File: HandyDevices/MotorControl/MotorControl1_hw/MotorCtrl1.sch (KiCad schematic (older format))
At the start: 20 parts, among them U1 L6470

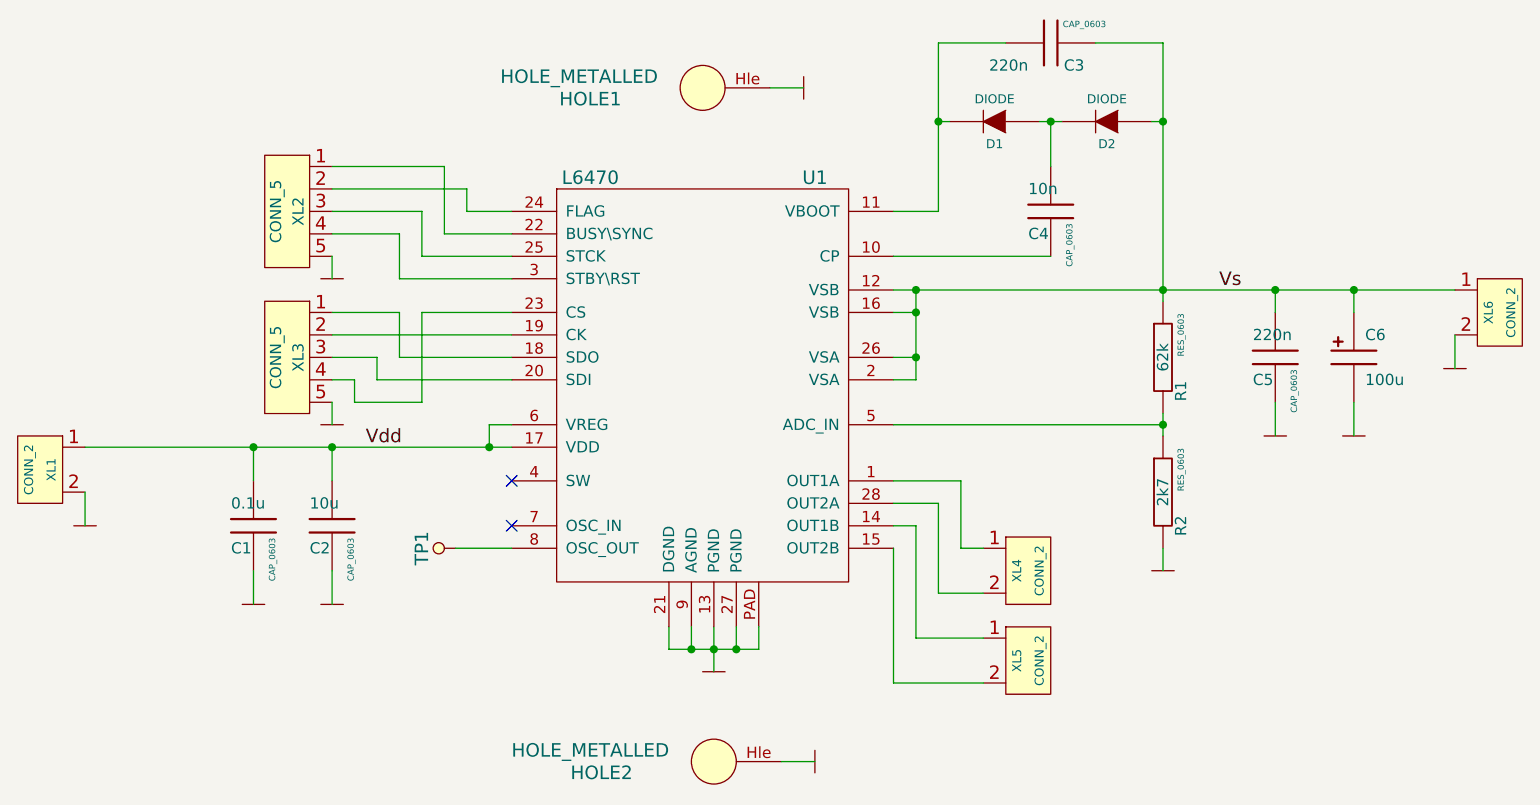
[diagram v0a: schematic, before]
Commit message: 
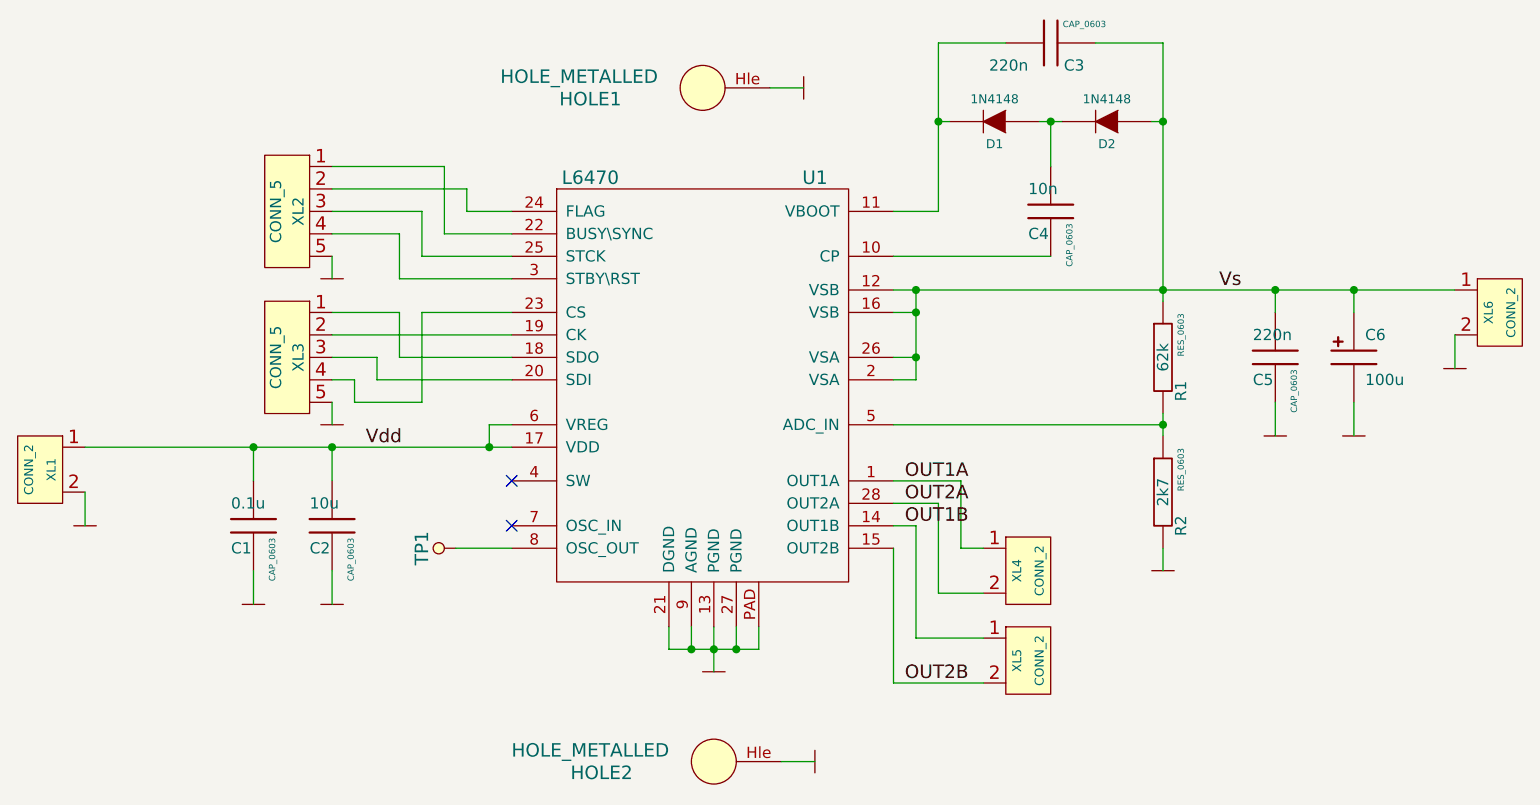
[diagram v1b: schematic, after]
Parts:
- D1, D2: value DIODE -> 1N4148
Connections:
- net OUT1A: now reaches U1.1 (OUT1A), XL4.1 (P1)
- net OUT1B: now reaches U1.14 (OUT1B), XL5.1 (P1)
- net OUT2B: now reaches U1.15 (OUT2B), XL5.2 (PM)
- net OUT2A: now reaches U1.28 (OUT2A), XL4.2 (PM)
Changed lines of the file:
@@
-EESchema Schematic File Version 2  date 4/10/2013 8:47:22 PM
+EESchema Schematic File Version 2  date 4/12/2013 6:02:38 PM
 LIBS:Connectors_kl
 LIBS:pcb_details
@@
 LIBS:st_kl
 LIBS:Tittar_kl
+LIBS:MotorCtrl1-cache
 EELAYER 27 0
 EELAYER END
@@
 Sheet 1 1
 Title ""
-Date "10 apr 2013"
+Date "12 apr 2013"
 Rev ""
 Comp ""
@@
 P 6750 2050
 F 0 "D1" H 6750 2150 40  0000 C CNN
-F 1 "DIODE" H 6750 1950 40  0000 C CNN
+F 1 "1N4148" H 6750 1950 40  0000 C CNN
 F 2 "" H 6750 2050 60  0000 C CNN
 F 3 "" H 6750 2050 60  0000 C CNN
@@
 P 7250 2050
 F 0 "D2" H 7250 2150 40  0000 C CNN
-F 1 "DIODE" H 7250 1950 40  0000 C CNN
+F 1 "1N4148" H 7250 1950 40  0000 C CNN
 F 2 "" H 7250 2050 60  0000 C CNN
 F 3 "" H 7250 2050 60  0000 C CNN
@@
 	8800 3000 8800 3150
 Connection ~ 8350 2800
+Text Label 6350 3650 0    60   ~ 0
+OUT1A
+Text Label 6350 3750 0    60   ~ 0
+OUT2A
+Text Label 6350 3850 0    60   ~ 0
+OUT1B
+Text Label 6350 4550 0    60   ~ 0
+OUT2B
 $EndSCHEMATC
